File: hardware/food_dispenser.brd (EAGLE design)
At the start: 45.4 x 44.4 mm, 7 parts, among them IC1 ESP-12E/F, IC2 1182-A4988

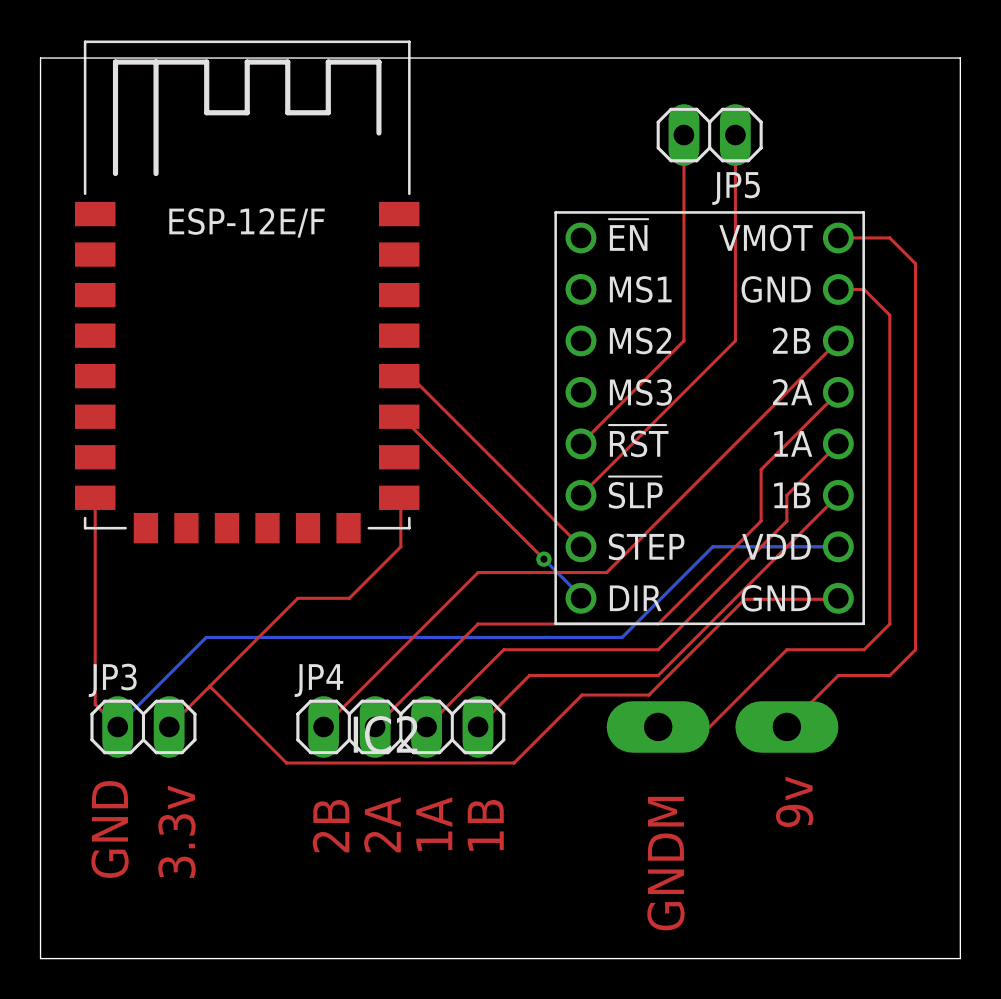
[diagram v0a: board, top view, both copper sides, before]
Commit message: feat: add gnd plate, pin names and logo to board
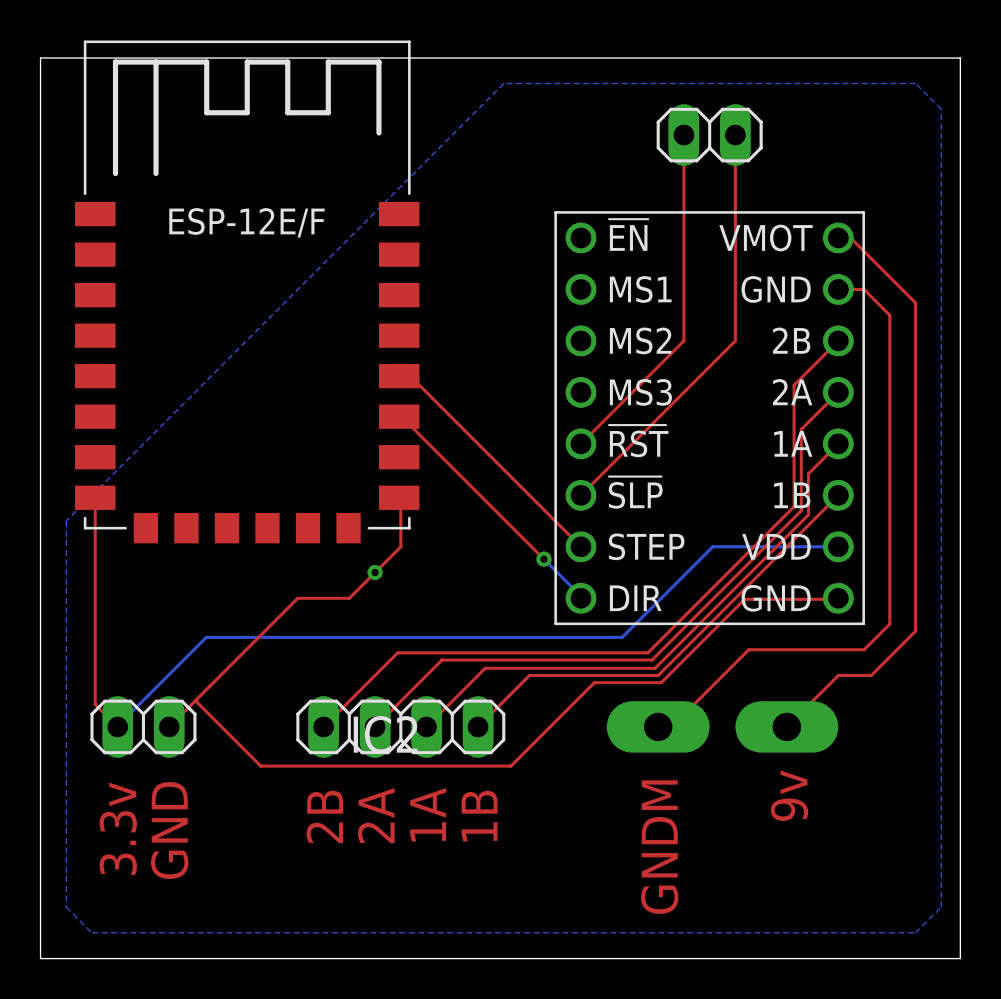
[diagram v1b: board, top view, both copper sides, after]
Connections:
- net N$4 renamed GND
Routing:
- net N$6: track 33.3 -> 36.8 mm
- net N$2: track 31.3 -> 29.6 mm
- net N$7: track 31.2 -> 32.0 mm
- net GND: track 53.5 -> 54.1 mm, vias 0 -> 1
- added copper zone on layer 16, net GND

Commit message: feat: add top gnd plate, via and fixation holes
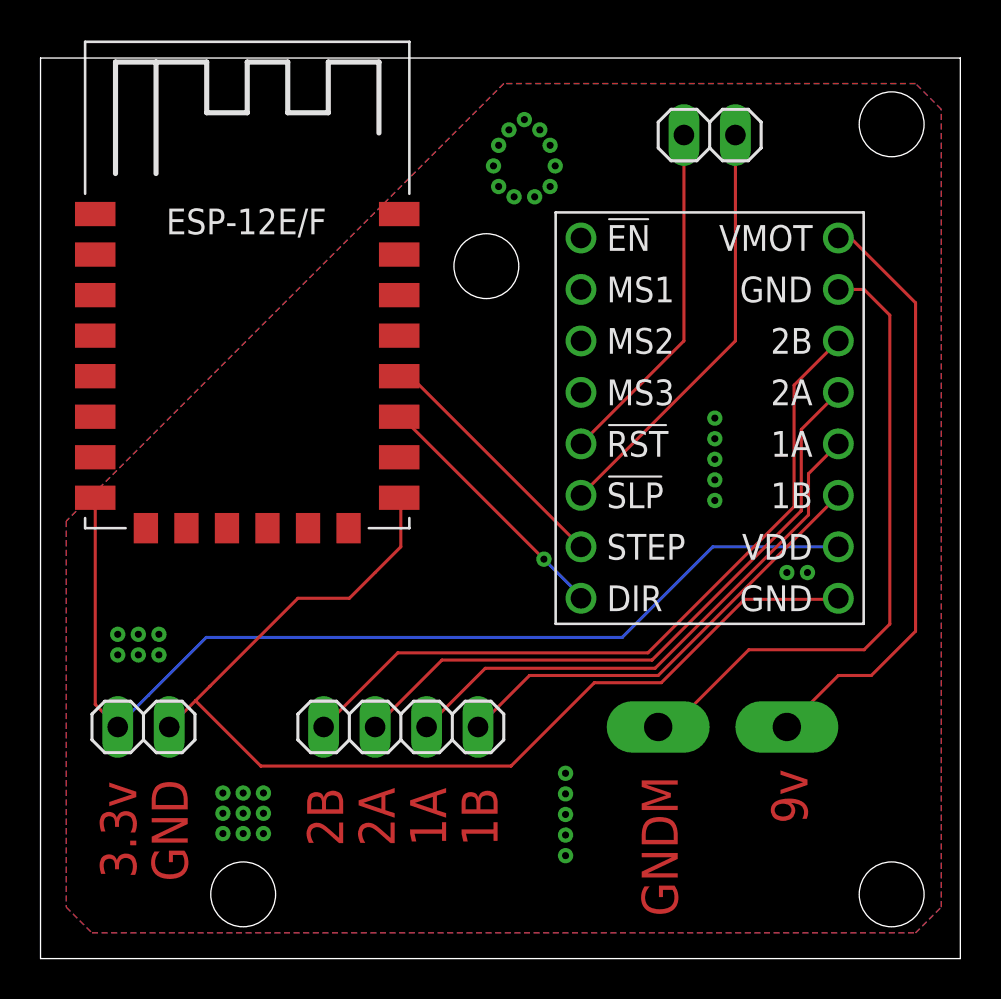
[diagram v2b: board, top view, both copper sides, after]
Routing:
- net GND: vias 1 -> 38
- added copper zone on layer 1, net GND
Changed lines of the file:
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@@
 <setting verticaltext="up"/>
 </settings>
-<grid distance="2" unitdist="mil" unit="mil" style="lines" multiple="1" display="yes" altdistance="5" altunitdist="mil" altunit="mil"/>
+<grid distance="1" unitdist="mm" unit="mm" style="lines" multiple="1" display="yes" altdistance="5" altunitdist="mil" altunit="mil"/>
 <layers>
 <layer number="1" name="Top" color="4" fill="1" visible="yes" active="yes"/>
@@
 <rectangle x1="6.731" y1="79.629" x2="6.985" y2="79.6798" layer="22"/>
 <rectangle x1="6.731" y1="79.6798" x2="6.9342" y2="79.7306" layer="22"/>
+<hole x="22" y="71" drill="3.2"/>
+<hole x="42" y="78" drill="3.2"/>
+<hole x="42" y="40" drill="3.2"/>
+<hole x="10" y="40" drill="3.2"/>
 </plain>
 <attributes>
@@
 <element name="IC1" library="esp-12e-f" package="ESP-12E" value="ESP-12E/F" x="10.16" y="66.04" smashed="yes"/>
 <element name="IC2" library="pololu-stepper-driver" package="A4988" value="1182-A4988" x="33.02" y="63.5" smashed="yes">
-<attribute name="NAME" x="15.24" y="46.99" size="1.778" layer="25"/>
 <attribute name="VALUE" x="27.305" y="74.295" size="1.778" layer="27"/>
 </element>
@@
 <wire x1="7.6454" y1="49.5554" x2="10.8712" y2="46.3296" width="0.1524" layer="1"/>
 <wire x1="39.3192" y1="54.5592" x2="39.37" y2="54.61" width="0.1524" layer="1"/>
-<via x="16.51" y="55.88" extent="1-16" drill="0.35"/>
+<polygon width="0.1524" layer="1">
+<vertex x="1.27" y="39.37"/>
+<vertex x="2.54" y="38.1"/>
+<vertex x="43.18" y="38.1"/>
+<vertex x="44.45" y="39.37"/>
+<vertex x="44.45" y="78.74"/>
+<vertex x="43.18" y="80.01"/>
+<vertex x="22.86" y="80.01"/>
+<vertex x="1.27" y="58.42"/>
+</polygon>
+<via x="5.842" y="51.816" extent="1-16" drill="0.35"/>
+<via x="4.826" y="51.816" extent="1-16" drill="0.35"/>
+<via x="3.81" y="51.816" extent="1-16" drill="0.35"/>
+<via x="5.842" y="52.832" extent="1-16" drill="0.35"/>
+<via x="4.826" y="52.832" extent="1-16" drill="0.35"/>
+<via x="3.81" y="52.832" extent="1-16" drill="0.35"/>
+<via x="9" y="43" extent="1-16" drill="0.35"/>
+<via x="10" y="43" extent="1-16" drill="0.35"/>
+<via x="11" y="43" extent="1-16" drill="0.35"/>
+<via x="11" y="44" extent="1-16" drill="0.35"/>
+<via x="10" y="44" extent="1-16" drill="0.35"/>
+<via x="9" y="44" extent="1-16" drill="0.35"/>
+<via x="9" y="45" extent="1-16" drill="0.35"/>
+<via x="10" y="45" extent="1-16" drill="0.35"/>
+<via x="11" y="45" extent="1-16" drill="0.35"/>
+<via x="25.908" y="41.91" extent="1-16" drill="0.35"/>
+<via x="25.908" y="42.926" extent="1-16" drill="0.35"/>
+<via x="25.908" y="43.942" extent="1-16" drill="0.35"/>
+<via x="25.908" y="44.958" extent="1-16" drill="0.35"/>
+<via x="25.908" y="45.974" extent="1-16" drill="0.35"/>
+<via x="33.274" y="59.436" extent="1-16" drill="0.35"/>
+<via x="33.274" y="60.452" extent="1-16" drill="0.35"/>
+<via x="33.274" y="61.468" extent="1-16" drill="0.35"/>
+<via x="33.274" y="62.484" extent="1-16" drill="0.35"/>
+<via x="33.274" y="63.5" extent="1-16" drill="0.35"/>
+<via x="36.83" y="55.88" extent="1-16" drill="0.35"/>
+<via x="37.846" y="55.88" extent="1-16" drill="0.35"/>
+<via x="23.368" y="74.422" extent="1-16" drill="0.35"/>
+<via x="22.606" y="74.93" extent="1-16" drill="0.35"/>
+<via x="22.352" y="75.946" extent="1-16" drill="0.35"/>
+<via x="24.384" y="74.422" extent="1-16" drill="0.35"/>
+<via x="25.146" y="74.93" extent="1-16" drill="0.35"/>
+<via x="25.4" y="75.946" extent="1-16" drill="0.35"/>
+<via x="25.146" y="76.962" extent="1-16" drill="0.35"/>
+<via x="22.606" y="76.962" extent="1-16" drill="0.35"/>
+<via x="23.114" y="77.724" extent="1-16" drill="0.35"/>
+<via x="23.876" y="78.232" extent="1-16" drill="0.35"/>
+<via x="24.638" y="77.724" extent="1-16" drill="0.35"/>
 </signal>
 </signals>
